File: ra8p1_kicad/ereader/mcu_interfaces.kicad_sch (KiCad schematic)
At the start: 1 part, among them U1 R7KA8P1KFLCAC#UC0

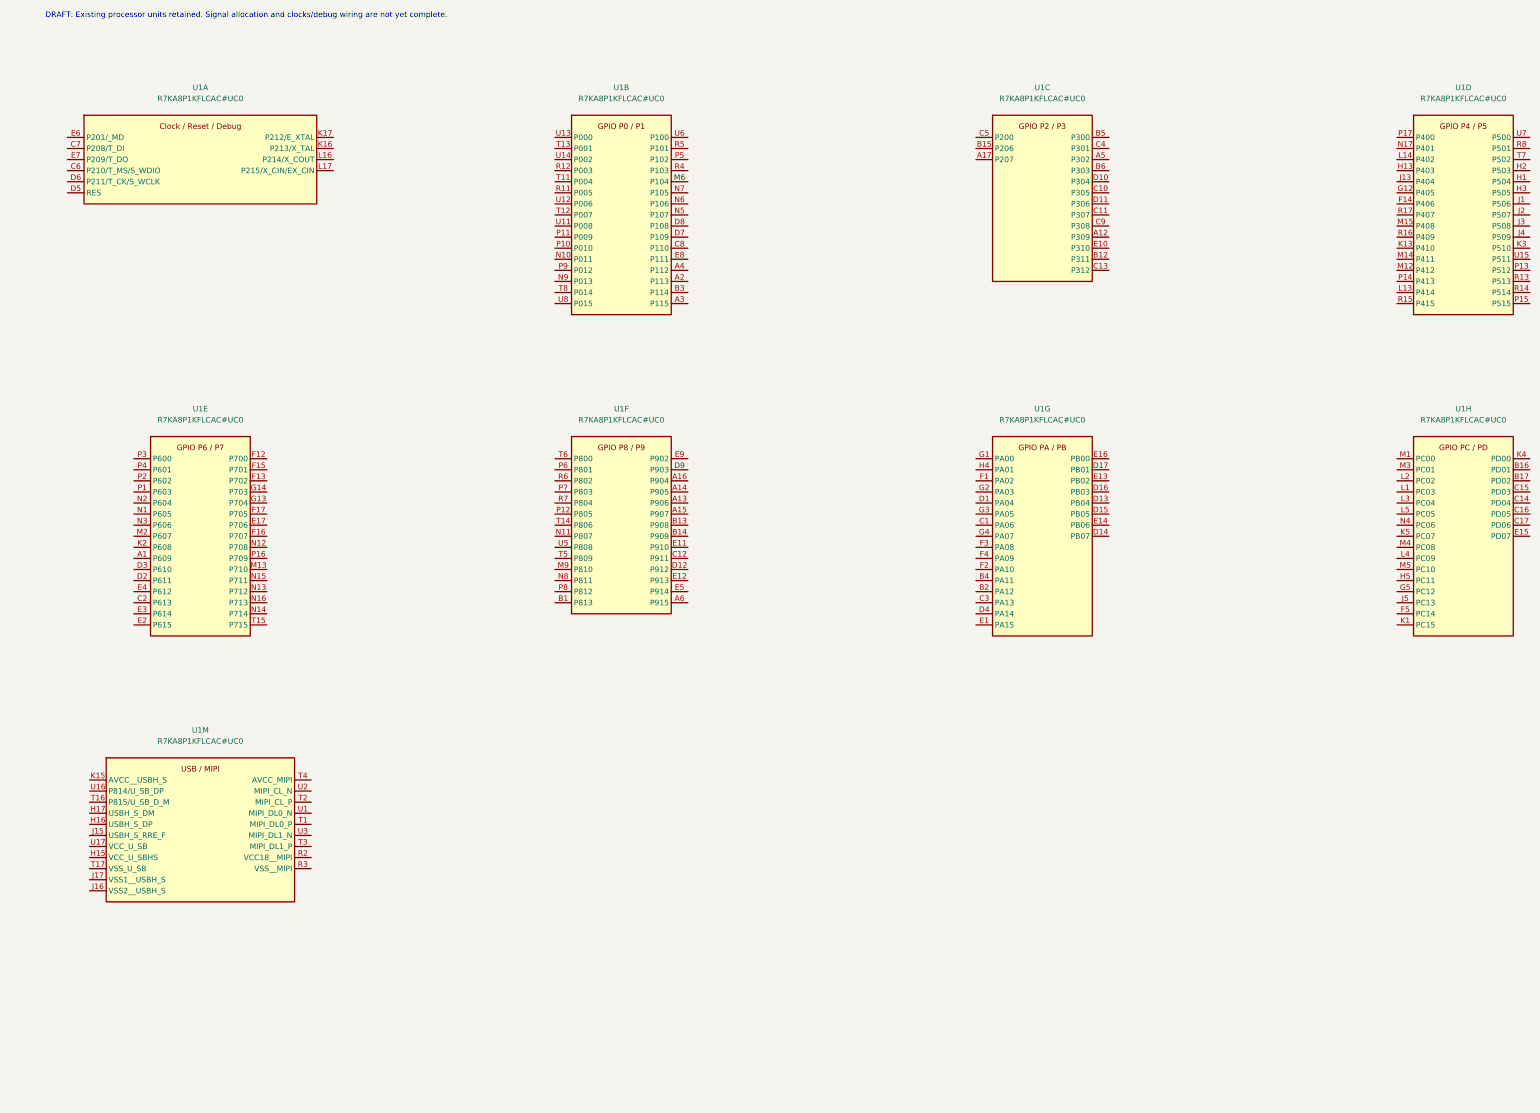
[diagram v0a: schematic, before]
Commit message: feat(hardware): add RA8P1 boot debug draft and refine schematic presentation
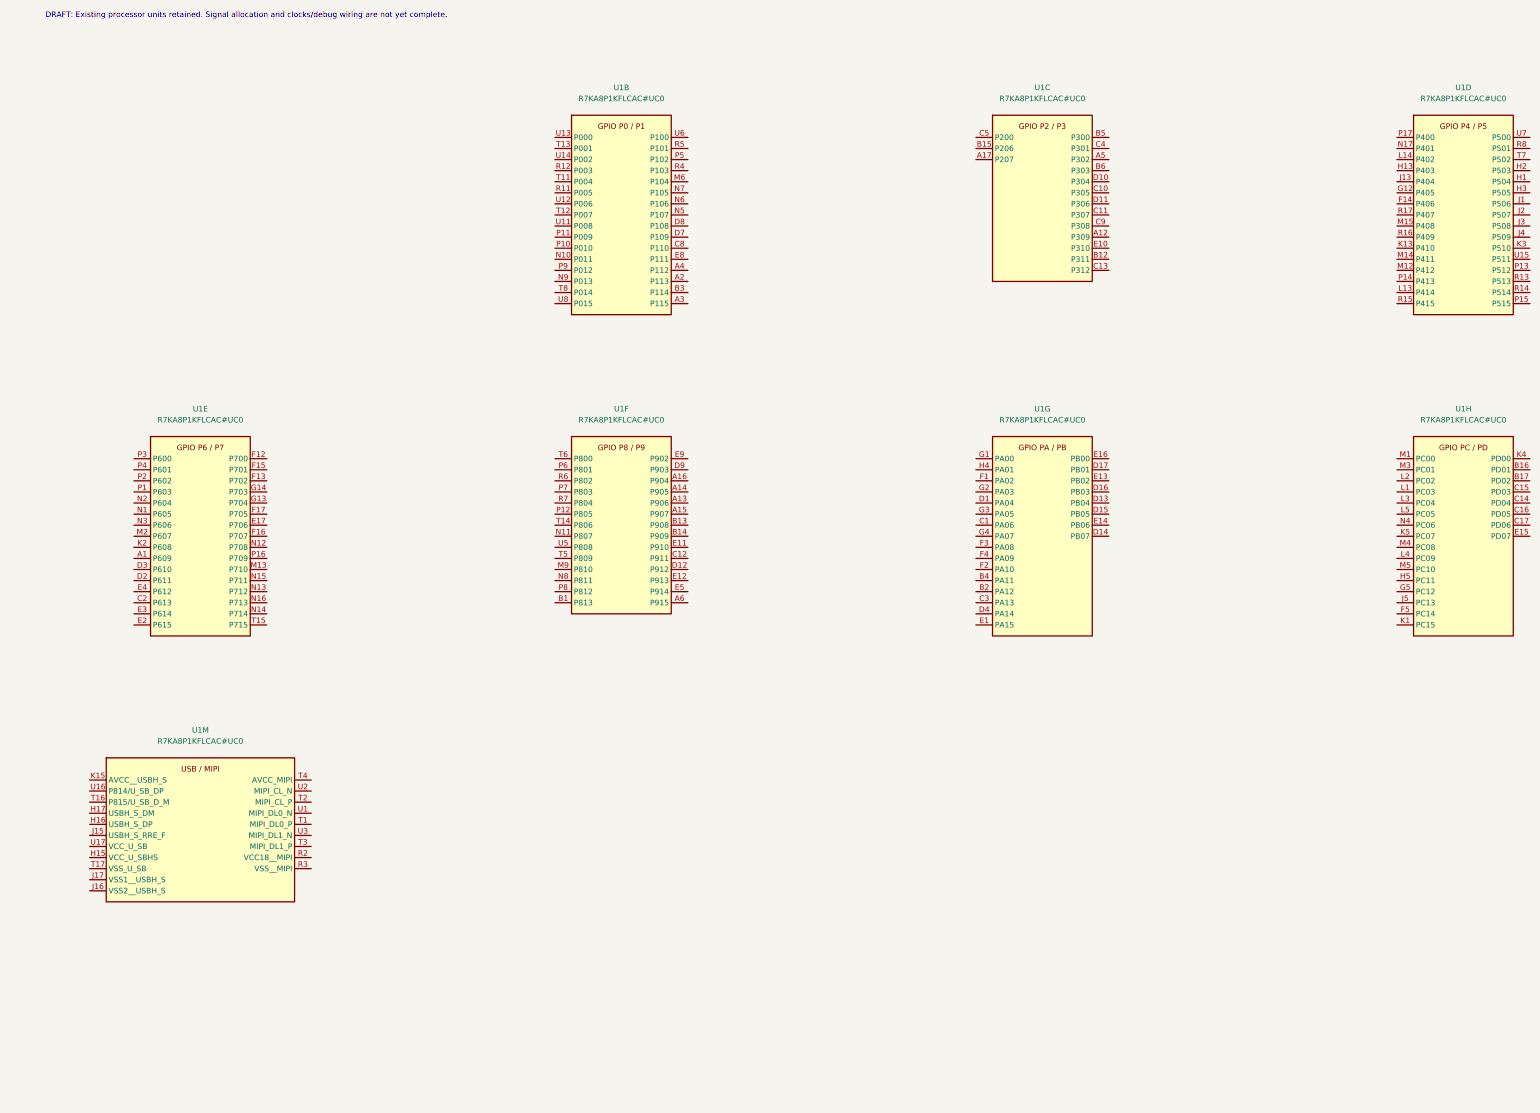
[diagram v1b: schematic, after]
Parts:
- removed unit 1 of U1
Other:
- title: RA8P1 clocks, debug and I/O allocation -> RA8P1 IO allocation

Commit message: feat(hardware): track schematic BOM and DigiKey sourcing risks
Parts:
- U1: DigiKey_Part_Number (none) -> 559-R7KA8P1KFLCAC#UC0-ND; DigiKey_URL (none) -> https://www.digikey.com/en/products/detail/renesas-electron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; Procurement_Status (none) -> HOLD - DigiKey discontinued; qualify orderable RA8P1 suffix; Sourcing_Snapshot (none) -> 2026-09-05 indexed: stock 1; USD 29.47; no backorders. Dist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

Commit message: feat(hardware): add Mouser sourcing and qualify MCU pull-up resistors
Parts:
- U1: Mouser Part Number (none) -> 968-R7KA8P1KFLCACUC0; Mouser Price/Stock (none) -> 2026-09-05 browser: 317 in stock; USD 1:29.47 / 10:23.82 / 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; Mouser_URL (none) -> https://www.mouser.com/en/ProductDetail/Renesas-Electronics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; Procurement_Status HOLD - DigiKey discontinued; qualify orderable RA8P1 suffix -> Retain exact UC0 - Mouser stock verified; circuit qualifica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
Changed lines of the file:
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@@
 			)
 		)
-		(property "Mouser Part Number" ""
+		(property "Mouser Part Number" "968-R7KA8P1KFLCACUC0"
 			(at 55.88 121.92 0)
 			(hide yes)
@@
 			)
 		)
-		(property "Mouser Price/Stock" ""
+		(property "Mouser Price/Stock" "2026-09-05 browser: 317 in stock; USD 1:29.47 / 10:23.82 / 25:22.75 / 100:21.71 / 189:21.70; MOQ 1, multiple 1. Recheck before order."
 			(at 55.88 121.92 0)
 			(hide yes)
@@
 			)
 		)
-		(property "Procurement_Status" "HOLD - DigiKey discontinued; qualify orderable RA8P1 suffix"
+		(property "Procurement_Status" "Retain exact UC0 - Mouser stock verified; circuit qualification ongoing"
 			(at 55.88 121.92 0)
 			(hide yes)
@@
 			)
 		)
+		(property "Mouser_URL" "https://www.mouser.com/en/ProductDetail/Renesas-Electronics/R7KA8P1KFLCACUC0?qs=2FehpBK1j97Anbj%252BfZIC1A%3D%3D"
+			(at 55.88 121.92 0)
+			(hide yes)
+			(show_name no)
+			(do_not_autoplace no)
+			(effects
+				(font
+					(size 1.27 1.27)
+				)
+			)
+		)
 		(pin "P3"
 		)
@@
 			)
 		)
-		(property "Mouser Part Number" ""
+		(property "Mouser Part Number" "968-R7KA8P1KFLCACUC0"
 			(at 248.92 48.26 0)
 			(hide yes)
@@
 			)
 		)
-		(property "Mouser Price/Stock" ""
+		(property "Mouser Price/Stock" "2026-09-05 browser: 317 in stock; USD 1:29.47 / 10:23.82 / 25:22.75 / 100:21.71 / 189:21.70; MOQ 1, multiple 1. Recheck before order."
 			(at 248.92 48.26 0)
 			(hide yes)
@@
 			)
 		)
-		(property "Procurement_Status" "HOLD - DigiKey discontinued; qualify orderable RA8P1 suffix"
+		(property "Procurement_Status" "Retain exact UC0 - Mouser stock verified; circuit qualification ongoing"
 			(at 248.92 48.26 0)
 			(hide yes)
@@
 			)
 		)
+		(property "Mouser_URL" "https://www.mouser.com/en/ProductDetail/Renesas-Electronics/R7KA8P1KFLCACUC0?qs=2FehpBK1j97Anbj%252BfZIC1A%3D%3D"
+			(at 248.92 48.26 0)
+			(hide yes)
+			(show_name no)
+			(do_not_autoplace no)
+			(effects
+				(font
+					(size 1.27 1.27)
+				)
+			)
+		)
 		(pin "C5"
 		)
@@
 			)
 		)
-		(property "Mouser Part Number" ""
+		(property "Mouser Part Number" "968-R7KA8P1KFLCACUC0"
 			(at 248.92 121.92 0)
 			(hide yes)
@@
 			)
 		)
-		(property "Mouser Price/Stock" ""
+		(property "Mouser Price/Stock" "2026-09-05 browser: 317 in stock; USD 1:29.47 / 10:23.82 / 25:22.75 / 100:21.71 / 189:21.70; MOQ 1, multiple 1. Recheck before order."
 			(at 248.92 121.92 0)
 			(hide yes)
@@
 			)
 		)
-		(property "Procurement_Status" "HOLD - DigiKey discontinued; qualify orderable RA8P1 suffix"
+		(property "Procurement_Status" "Retain exact UC0 - Mouser stock verified; circuit qualification ongoing"
 			(at 248.92 121.92 0)
 			(hide yes)
@@
 			)
 		)
+		(property "Mouser_URL" "https://www.mouser.com/en/ProductDetail/Renesas-Electronics/R7KA8P1KFLCACUC0?qs=2FehpBK1j97Anbj%252BfZIC1A%3D%3D"
+			(at 248.92 121.92 0)
+			(hide yes)
+			(show_name no)
+			(do_not_autoplace no)
+			(effects
+				(font
+					(size 1.27 1.27)
+				)
+			)
+		)
 		(pin "G1"
 		)
@@
 			)
 		)
-		(property "Mouser Part Number" ""
+		(property "Mouser Part Number" "968-R7KA8P1KFLCACUC0"
 			(at 152.4 121.92 0)
 			(hide yes)
@@
 			)
 		)
-		(property "Mouser Price/Stock" ""
+		(property "Mouser Price/Stock" "2026-09-05 browser: 317 in stock; USD 1:29.47 / 10:23.82 / 25:22.75 / 100:21.71 / 189:21.70; MOQ 1, multiple 1. Recheck before order."
 			(at 152.4 121.92 0)
 			(hide yes)
@@
 			)
 		)
-		(property "Procurement_Status" "HOLD - DigiKey discontinued; qualify orderable RA8P1 suffix"
+		(property "Procurement_Status" "Retain exact UC0 - Mouser stock verified; circuit qualification ongoing"
 			(at 152.4 121.92 0)
 			(hide yes)
@@
 			)
 		)
+		(property "Mouser_URL" "https://www.mouser.com/en/ProductDetail/Renesas-Electronics/R7KA8P1KFLCACUC0?qs=2FehpBK1j97Anbj%252BfZIC1A%3D%3D"
+			(at 152.4 121.92 0)
+			(hide yes)
+			(show_name no)
+			(do_not_autoplace no)
+			(effects
+				(font
+					(size 1.27 1.27)
+				)
+			)
+		)
 		(pin "T6"
 		)
@@
 			)
 		)
-		(property "Mouser Part Number" ""
+		(property "Mouser Part Number" "968-R7KA8P1KFLCACUC0"
 			(at 152.4 48.26 0)
 			(hide yes)
@@
 			)
 		)
-		(property "Mouser Price/Stock" ""
+		(property "Mouser Price/Stock" "2026-09-05 browser: 317 in stock; USD 1:29.47 / 10:23.82 / 25:22.75 / 100:21.71 / 189:21.70; MOQ 1, multiple 1. Recheck before order."
 			(at 152.4 48.26 0)
 			(hide yes)
@@
 			)
 		)
-		(property "Procurement_Status" "HOLD - DigiKey discontinued; qualify orderable RA8P1 suffix"
+		(property "Procurement_Status" "Retain exact UC0 - Mouser stock verified; circuit qualification ongoing"
 			(at 152.4 48.26 0)
 			(hide yes)
@@
 			)
 		)
+		(property "Mouser_URL" "https://www.mouser.com/en/ProductDetail/Renesas-Electronics/R7KA8P1KFLCACUC0?qs=2FehpBK1j97Anbj%252BfZIC1A%3D%3D"
+			(at 152.4 48.26 0)
+			(hide yes)
+			(show_name no)
+			(do_not_autoplace no)
+			(effects
+				(font
+					(size 1.27 1.27)
+				)
+			)
+		)
 		(pin "U13"
 		)
@@
 			)
 		)
-		(property "Mouser Part Number" ""
+		(property "Mouser Part Number" "968-R7KA8P1KFLCACUC0"
 			(at 345.44 121.92 0)
 			(hide yes)
@@
 			)
 		)
-		(property "Mouser Price/Stock" ""
+		(property "Mouser Price/Stock" "2026-09-05 browser: 317 in stock; USD 1:29.47 / 10:23.82 / 25:22.75 / 100:21.71 / 189:21.70; MOQ 1, multiple 1. Recheck before order."
 			(at 345.44 121.92 0)
 			(hide yes)
@@
 			)
 		)
-		(property "Procurement_Status" "HOLD - DigiKey discontinued; qualify orderable RA8P1 suffix"
+		(property "Procurement_Status" "Retain exact UC0 - Mouser stock verified; circuit qualification ongoing"
 			(at 345.44 121.92 0)
 			(hide yes)
@@
 			)
 		)
+		(property "Mouser_URL" "https://www.mouser.com/en/ProductDetail/Renesas-Electronics/R7KA8P1KFLCACUC0?qs=2FehpBK1j97Anbj%252BfZIC1A%3D%3D"
+			(at 345.44 121.92 0)
+			(hide yes)
+			(show_name no)
+			(do_not_autoplace no)
+			(effects
+				(font
+					(size 1.27 1.27)
+				)
+			)
+		)
 		(pin "M1"
 		)
@@
 			)
 		)
-		(property "Mouser Part Number" ""
+		(property "Mouser Part Number" "968-R7KA8P1KFLCACUC0"
 			(at 345.44 48.26 0)
 			(hide yes)
@@
 			)
 		)
-		(property "Mouser Price/Stock" ""
+		(property "Mouser Price/Stock" "2026-09-05 browser: 317 in stock; USD 1:29.47 / 10:23.82 / 25:22.75 / 100:21.71 / 189:21.70; MOQ 1, multiple 1. Recheck before order."
 			(at 345.44 48.26 0)
 			(hide yes)
@@
 			)
 		)
-		(property "Procurement_Status" "HOLD - DigiKey discontinued; qualify orderable RA8P1 suffix"
+		(property "Procurement_Status" "Retain exact UC0 - Mouser stock verified; circuit qualification ongoing"
 			(at 345.44 48.26 0)
 			(hide yes)
@@
 			)
 		)
+		(property "Mouser_URL" "https://www.mouser.com/en/ProductDetail/Renesas-Electronics/R7KA8P1KFLCACUC0?qs=2FehpBK1j97Anbj%252BfZIC1A%3D%3D"
+			(at 345.44 48.26 0)
+			(hide yes)
+			(show_name no)
+			(do_not_autoplace no)
+			(effects
+				(font
+					(size 1.27 1.27)
+				)
+			)
+		)
 		(pin "P17"
 		)
@@
 			)
 		)
-		(property "Mouser Part Number" ""
+		(property "Mouser Part Number" "968-R7KA8P1KFLCACUC0"
 			(at 55.88 195.58 0)
 			(hide yes)
@@
 			)
 		)
-		(property "Mouser Price/Stock" ""
+		(property "Mouser Price/Stock" "2026-09-05 browser: 317 in stock; USD 1:29.47 / 10:23.82 / 25:22.75 / 100:21.71 / 189:21.70; MOQ 1, multiple 1. Recheck before order."
 			(at 55.88 195.58 0)
 			(hide yes)
@@
 			)
 		)
-		(property "Procurement_Status" "HOLD - DigiKey discontinued; qualify orderable RA8P1 suffix"
+		(property "Procurement_Status" "Retain exact UC0 - Mouser stock verified; circuit qualification ongoing"
 			(at 55.88 195.58 0)
 			(hide yes)
@@
 			(at 55.88 195.58 0)
 			(hide yes)
+			(show_name no)
+			(do_not_autoplace no)
+			(effects
+				(font
+					(size 1.27 1.27)
+				)
+			)
+		)
+		(property "Mouser_URL" "https://www.mouser.com/en/ProductDetail/Renesas-Electronics/R7KA8P1KFLCACUC0?qs=2FehpBK1j97Anbj%252BfZIC1A%3D%3D"
+			(at 55.88 195.58 0)
+			(hide yes)

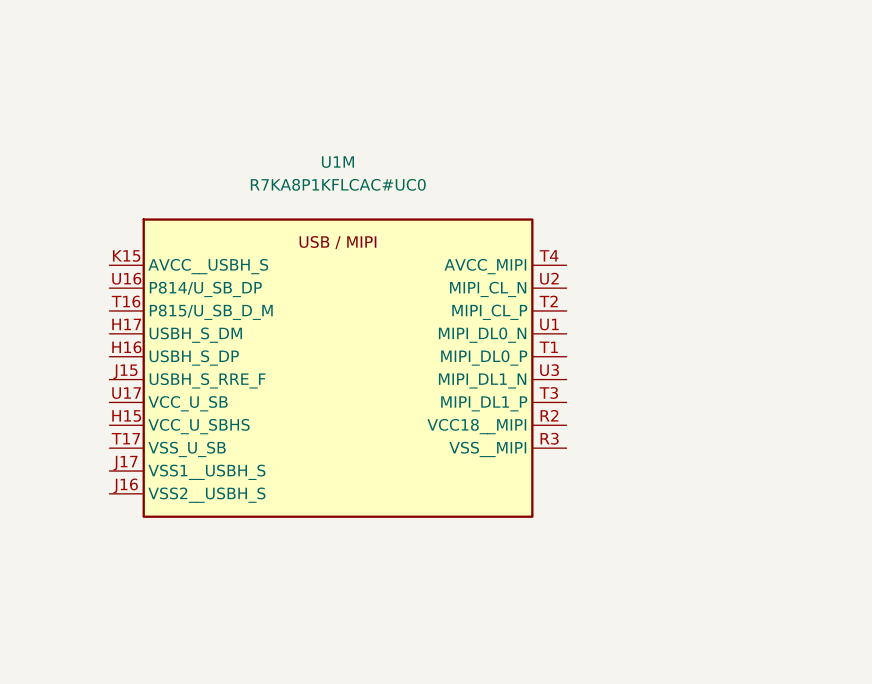
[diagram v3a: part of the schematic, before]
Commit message: feat(hardware): terminate unused RA8P1 MIPI interface
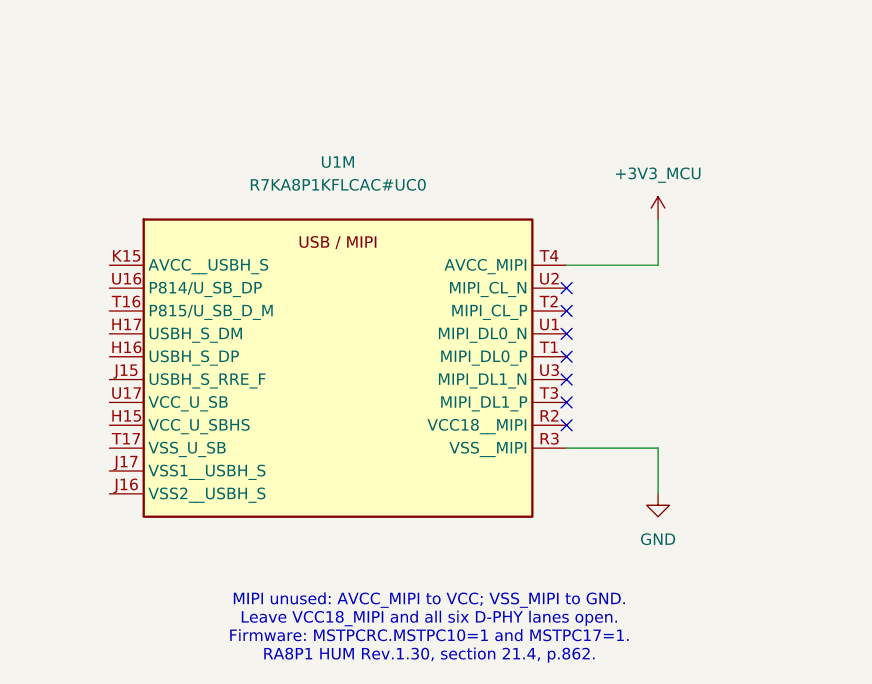
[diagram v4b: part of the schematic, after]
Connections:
- net GND: now reaches U1.R3 (VSS__MIPI)
- net +3V3_MCU: now reaches U1.T4 (AVCC_MIPI)
- no-connect marks 0 -> 7
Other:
- note added: "MIPI unused: AVCC_MIPI to VCC; VSS_MIPI to GND. Leave VCC18_MIPI and all six D-PHY lanes open. Firmware: MSTPCRC.MSTPC10=1 and MSTPC17=1. RA8P1 HUM Rev.1.30, section 21.4, p.862."
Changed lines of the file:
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@@
 		)
 	)
+	(text "MIPI unused: AVCC_MIPI to VCC; VSS_MIPI to GND.\nLeave VCC18_MIPI and all six D-PHY lanes open.\nFirmware: MSTPCRC.MSTPC10=1 and MSTPC17=1.\nRA8P1 HUM Rev.1.30, section 21.4, p.862."
+		(exclude_from_sim no)
+		(at 66.04 235.966 0)
+		(effects
+			(font
+				(size 1.27 1.27)
+			)
+		)
+	)
+	(no_connect
+		(at 81.28 213.36)
+	)
+	(no_connect
+		(at 81.28 205.74)
+	)
+	(no_connect
+		(at 81.28 198.12)
+	)
+	(no_connect
+		(at 81.28 203.2)
+	)
+	(no_connect
+		(at 81.28 210.82)
+	)
+	(no_connect
+		(at 81.28 208.28)
+	)
+	(no_connect
+		(at 81.28 200.66)
+	)
+	(wire
+		(pts
+			(xy 81.28 215.9) (xy 91.44 215.9)
+		)
+		(stroke
+			(width 0)
+			(type default)
+		)
+	)
+	(wire
+		(pts
+			(xy 91.44 190.5) (xy 91.44 195.58)
+		)
+		(stroke
+			(width 0)
+			(type default)
+		)
+	)
+	(wire
+		(pts
+			(xy 91.44 220.98) (xy 91.44 215.9)
+		)
+		(stroke
+			(width 0)
+			(type default)
+		)
+	)
+	(wire
+		(pts
+			(xy 81.28 195.58) (xy 91.44 195.58)
+		)
+		(stroke
+			(width 0)
+			(type default)
+		)
+	)
 	(symbol
 		(lib_id "Processors:R7KA8P1KFLCAC#UC0")
@@
 	)
 	(symbol
+		(lib_id "power:GND")
+		(at 91.44 220.98 0)
+		(unit 1)
+		(body_style 1)
+		(exclude_from_sim no)
+		(in_bom yes)
+		(on_board yes)
+		(in_pos_files yes)
+		(dnp no)
+		(fields_autoplaced yes)
+		(property "Reference" "#PWR034"
+			(at 91.44 227.33 0)
+			(hide yes)
+			(show_name no)
+			(do_not_autoplace no)
+			(effects
+				(font
+					(size 1.27 1.27)
+				)
+			)
+		)
+		(property "Value" "GND"
+			(at 91.44 226.06 0)
+			(show_name no)
+			(do_not_autoplace no)
+			(effects
+				(font
+					(size 1.27 1.27)
+				)
+			)
+		)
+		(property "Footprint" ""
+			(at 91.44 220.98 0)
+			(hide yes)
+			(show_name no)
+			(do_not_autoplace no)
+			(effects
+				(font
+					(size 1.27 1.27)
+				)
+			)
+		)
+		(property "Datasheet" ""
+			(at 91.44 220.98 0)
+			(hide yes)
+			(show_name no)
+			(do_not_autoplace no)
+			(effects
+				(font
+					(size 1.27 1.27)
+				)
+			)
+		)
+		(property "Description" "Power symbol creates a global label with name \"GND\" , ground"
+			(at 91.44 220.98 0)
+			(hide yes)
+			(show_name no)
+			(do_not_autoplace no)
+			(effects
+				(font
+					(size 1.27 1.27)
+				)
+			)
+		)
+		(pin "1"
+		)
+		(instances
+			(project "ereader_rev1"
+				(path "/0586cc51-9c57-495b-a0c9-c29ba0d48166/33c39500-46ef-4bfe-91bb-bf0f803ca6e5"
+					(reference "#PWR034")
+					(unit 1)
+				)
+			)
+		)
+	)
+	(symbol
 		(lib_id "Processors:R7KA8P1KFLCAC#UC0")
 		(at 345.44 121.92 0)
@@
 				)
 			)
+		)
+	)
+	(symbol
+		(lib_id "power:+3V3")
+		(at 91.44 190.5 0)
+		(unit 1)
+		(body_style 1)
+		(exclude_from_sim no)
+		(in_bom yes)
+		(on_board yes)
+		(in_pos_files yes)
+		(dnp no)
+		(fields_autoplaced yes)
+		(property "Reference" "#PWR035"
+			(at 91.44 194.31 0)
+			(hide yes)
+			(show_name no)
+			(do_not_autoplace no)
+			(effects
+				(font
+					(size 1.27 1.27)
+				)
+			)
+		)
+		(property "Value" "+3V3_MCU"
+			(at 91.44 185.42 0)
+			(show_name no)
+			(do_not_autoplace no)
+			(effects
+				(font
+					(size 1.27 1.27)
+				)
+			)
+		)
+		(property "Footprint" ""
+			(at 91.44 190.5 0)
+			(hide yes)
+			(show_name no)
+			(do_not_autoplace no)
+			(effects
+				(font
+					(size 1.27 1.27)
+				)
+			)
+		)
+		(property "Datasheet" ""
+			(at 91.44 190.5 0)
+			(hide yes)
+			(show_name no)
+			(do_not_autoplace no)
+			(effects
+				(font
+					(size 1.27 1.27)
+				)
+			)
+		)
+		(property "Description" "Power symbol creates a global label with name \"+3V3\""
+			(at 91.44 190.5 0)
+			(hide yes)
+			(show_name no)
+			(do_not_autoplace no)
+			(effects
+				(font
+					(size 1.27 1.27)
+				)
+			)
+		)
+		(pin "1"
+		)
+		(instances
+			(project "ereader_rev1"
+				(path "/0586cc51-9c57-495b-a0c9-c29ba0d48166/33c39500-46ef-4bfe-91bb-bf0f803ca6e5"
+					(reference "#PWR035")
+					(unit 1)
+				)
+			)
